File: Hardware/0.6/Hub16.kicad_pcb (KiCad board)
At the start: 2 copper layers, 89 x 100 mm, 120 parts, among them J1 USB_C_Receptacle_USB2.0, J2 AVR-ISP-6, J3 USB_C_Receptacle_USB2.0, J4 USB_C_Receptacle_USB2.0, J5 USB_C_Receptacle_USB2.0, K1 KEYSW, K11 KEYSW, K12 KEYSW, K13 KEYSW, K14 KEYSW, K16 KEYSW, K17 KEYSW, K18 KEYSW, K19 KEYSW, K2 KEYSW, K3 KEYSW, K4 KEYSW, K6 KEYSW, K7 KEYSW, K8 KEYSW, K9 KEYSW, SW1 KMR2, SW2 Rotary_Encoder_Switch, SW3 Rotary_Encoder_Switch, U1 USBLC6-2SC6, U2 ATMEGA32U4, U3 CY7C65632-28LTXCT, U4 USBLC6-2SC6, U5 USBLC6-2SC6, U6 USBLC6-2SC6, Y1 16MHz, Y2 12MHz

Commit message: more layout
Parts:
- LOGO3: value Rev 0.6 -> Board-Details
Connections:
- U4 pad 1: /USB Hub/D3_D- -> Net-(J5-PadA7)
- U4 pad 3: /USB Hub/D3_D+ -> Net-(J5-PadA6)
- U4 pad 4: Net-(J5-PadA6) -> /USB Hub/D3_D+
- U4 pad 6: Net-(J5-PadA7) -> /USB Hub/D3_D-
- U5 pad 1: /USB Hub/D1_D+ -> Net-(J4-PadA7)
- U5 pad 3: /USB Hub/D1_D- -> Net-(J4-PadA6)
- U5 pad 4: Net-(J4-PadA7) -> /USB Hub/D1_D+
- U5 pad 6: Net-(J4-PadA6) -> /USB Hub/D1_D-
- U6 pad 1: /USB Hub/D2_D- -> Net-(J3-PadA7)
- U6 pad 3: /USB Hub/D2_D+ -> Net-(J3-PadA6)
- U6 pad 4: Net-(J3-PadA6) -> /USB Hub/D2_D+
- U6 pad 6: Net-(J3-PadA7) -> /USB Hub/D2_D-
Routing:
- net +5V: track 19.0 -> 22.1 mm, vias 5 -> 7
- net /row1: track 84.4 -> 85.2 mm
- net /col3: track 67.4 -> 66.7 mm

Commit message: update gitignore
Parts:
- removed C23: 1u, Capacitor_SMD:C_0603_1608Metric
- removed R13: 100K, Resistor_SMD:R_0603_1608Metric
- C12: value 100n -> 10u
- C13: value 10u -> 100n
- F2, F3, F4: value 500mA -> 200mA
- LOGO3: value Board-Details -> Rev 0.6
- R10: value 47K -> 10K
- R9: value 100K -> 10K
- moved R10 1.08 mm to (81.4, 62.7)
- moved R12 0.41 mm to (79.9, 62.7), turned to 270 degrees
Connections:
- R10 pad 1: Net-(C23-Pad1) -> Net-(R10-Pad1)
- R10 pad 2: GND -> +3V3
- R12 pad 1: +5V -> Net-(R12-Pad1)
- R12 pad 2: Net-(C23-Pad1) -> +3V3
- U3 pad 17: Net-(C23-Pad1) -> Net-(R10-Pad1)
- U3 pad 22: Net-(R13-Pad1) -> Net-(R12-Pad1)
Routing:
- net Net-(C23-Pad1): track 16.0 -> 0.00 mm, vias 2 -> 0
- net Net-(R10-Pad1): track 0.00 -> 13.2 mm, vias 0 -> 2
- net Net-(R13-Pad1): track 10.6 -> 0.00 mm, vias 2 -> 0
- net Net-(R12-Pad1): track 0.00 -> 9.39 mm, vias 0 -> 2
- net +3V3: track 28.6 -> 34.7 mm
- net GND: track 79.6 -> 77.2 mm, vias 78 -> 75

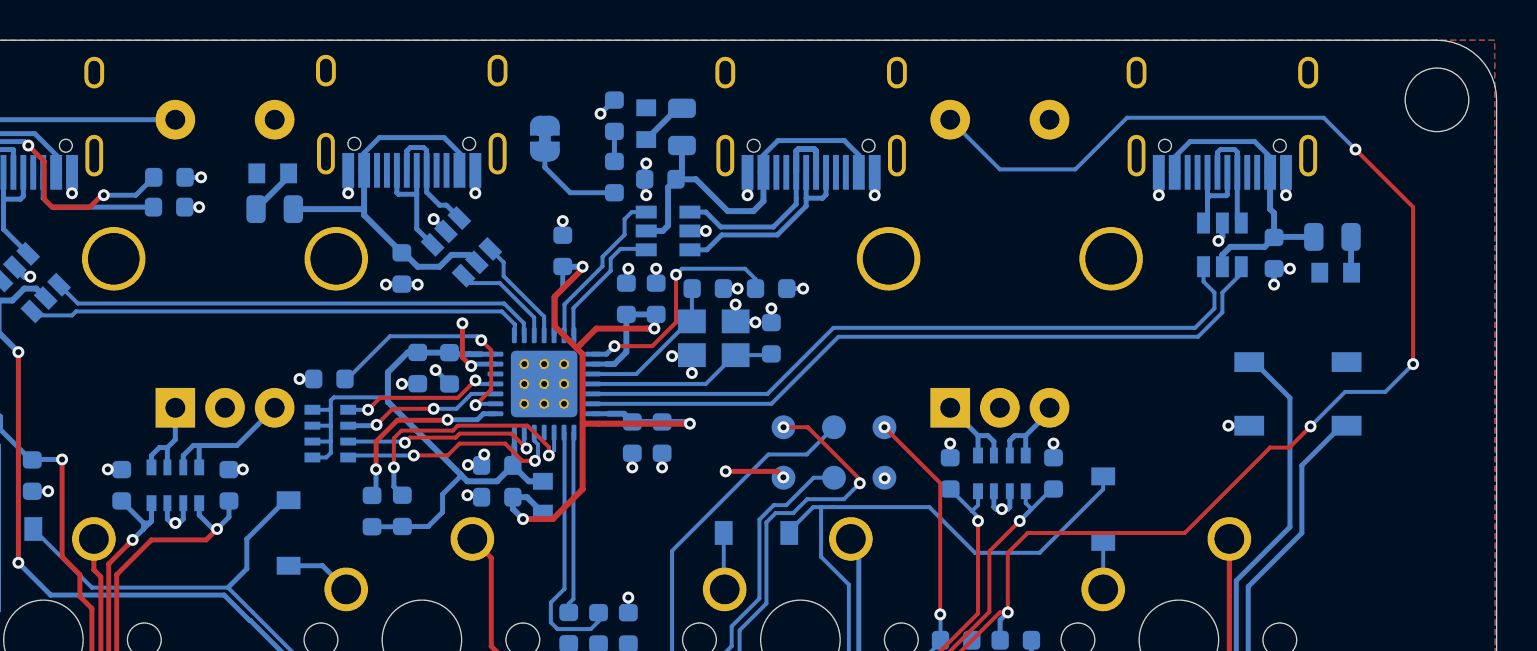
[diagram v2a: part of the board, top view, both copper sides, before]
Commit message: clean up routing, should probably start USB hub from scratch...
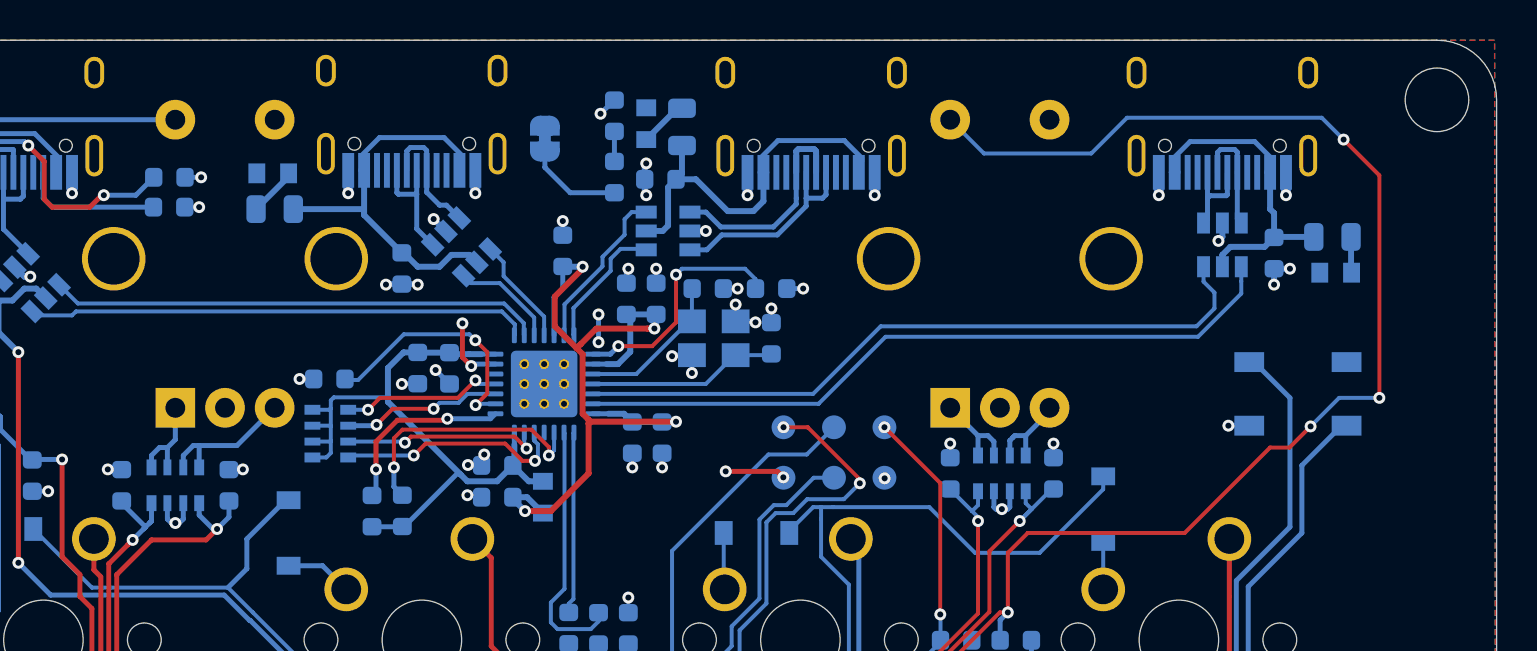
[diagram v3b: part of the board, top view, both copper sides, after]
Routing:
- net /ENC_2_SW: track 91.1 -> 89.0 mm
- net +3.3VA: track 44.8 -> 42.7 mm
- net GND: track 77.2 -> 78.6 mm, vias 75 -> 77
- net +3V3: track 34.7 -> 34.0 mm

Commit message: laid out USB hub from scratch, much better
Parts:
- added FB5: 600R, josh-passives-smt:Ferrite_Bead_0603, B.Cu at (57.9, 51.5)
- LOGO3: value Rev 0.6 -> Board-Details
- R1: value 2K2 -> 5K1
- moved FB4 13.2 mm to (88.0, 47.5), turned to 90 degrees
- moved F3 10.6 mm to (85.4, 49.5), turned to 0 degrees
- moved C22 10.5 mm to (87.8, 64.4), turned to 0 degrees
- moved C21 8.32 mm to (87.8, 62.8), turned to 0 degrees
- moved FB1 7.46 mm to (82.4, 57.7), turned to 0 degrees
- moved C12 5.67 mm to (82.4, 56.2)
- moved R9 5.02 mm to (78.6, 61.0)
- moved F4 4.74 mm to (95.5, 48.1), turned to 180 degrees
- moved C13 4.71 mm to (82.4, 59.2), turned to 0 degrees
- moved C26 4.69 mm to (98.7, 47.9)
- moved C25 4.66 mm to (85.2, 47.8), turned to 0 degrees
- moved U6 4.19 mm to (98.3, 50.9)
- moved C20 3.67 mm to (92.9, 62.3), turned to 0 degrees
- moved JP11 3.66 mm to (92.0, 45.3), turned to 180 degrees
- moved FB2 3.49 mm to (95.3, 46.3), turned to 0 degrees
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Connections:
- F1 pad 1: +5V -> Net-(F1-Pad1)
- U2 pad 2: VBUS -> +5V
- U2 pad 7: VBUS -> +5V
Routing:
- net VBUS: track 71.8 -> 15.7 mm, vias 2 -> 0
- net +3.3VA: track 42.7 -> 54.3 mm, vias 4 -> 5
- net GND: track 78.6 -> 89.4 mm, vias 77 -> 70
- net +3V3: track 34.0 -> 41.7 mm
- net +5V: track 22.1 -> 15.9 mm, vias 7 -> 5
- net /row1: track 85.2 -> 91.1 mm
- net /row2: track 72.2 -> 66.8 mm
- net /USB Hub/UP_USB_P: track 24.8 -> 29.7 mm
- net /USB Hub/UP_USB_N: track 25.3 -> 29.9 mm
- net /ENC_1_SW: track 78.0 -> 82.5 mm
- net Net-(R9-Pad1): track 12.4 -> 8.17 mm
- net /USB Hub/D2_D+: track 6.68 -> 10.7 mm
- net Net-(C25-Pad1): track 19.5 -> 15.6 mm
- net Net-(R10-Pad1): track 13.1 -> 16.9 mm
- net /USB Hub/D1_D-: track 5.32 -> 9.05 mm
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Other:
- net class Power added: clearance 0.15, trace_width 0.25, via_dia 0.6, via_drill 0.3
